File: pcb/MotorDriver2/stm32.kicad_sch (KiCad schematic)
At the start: 29 parts, among them IC1 STM32C092RCT6, J1 GT-USB-7010ASV, SW1 K2-6639SP-C4SC-04, SW2 K2-6639SP-C4SC-04, SW3 K2-6639SP-C4SC-04, U1 NCP361SNT1G, U2 CH340X, Y1 48 MHz, Y2 32.768 kHz

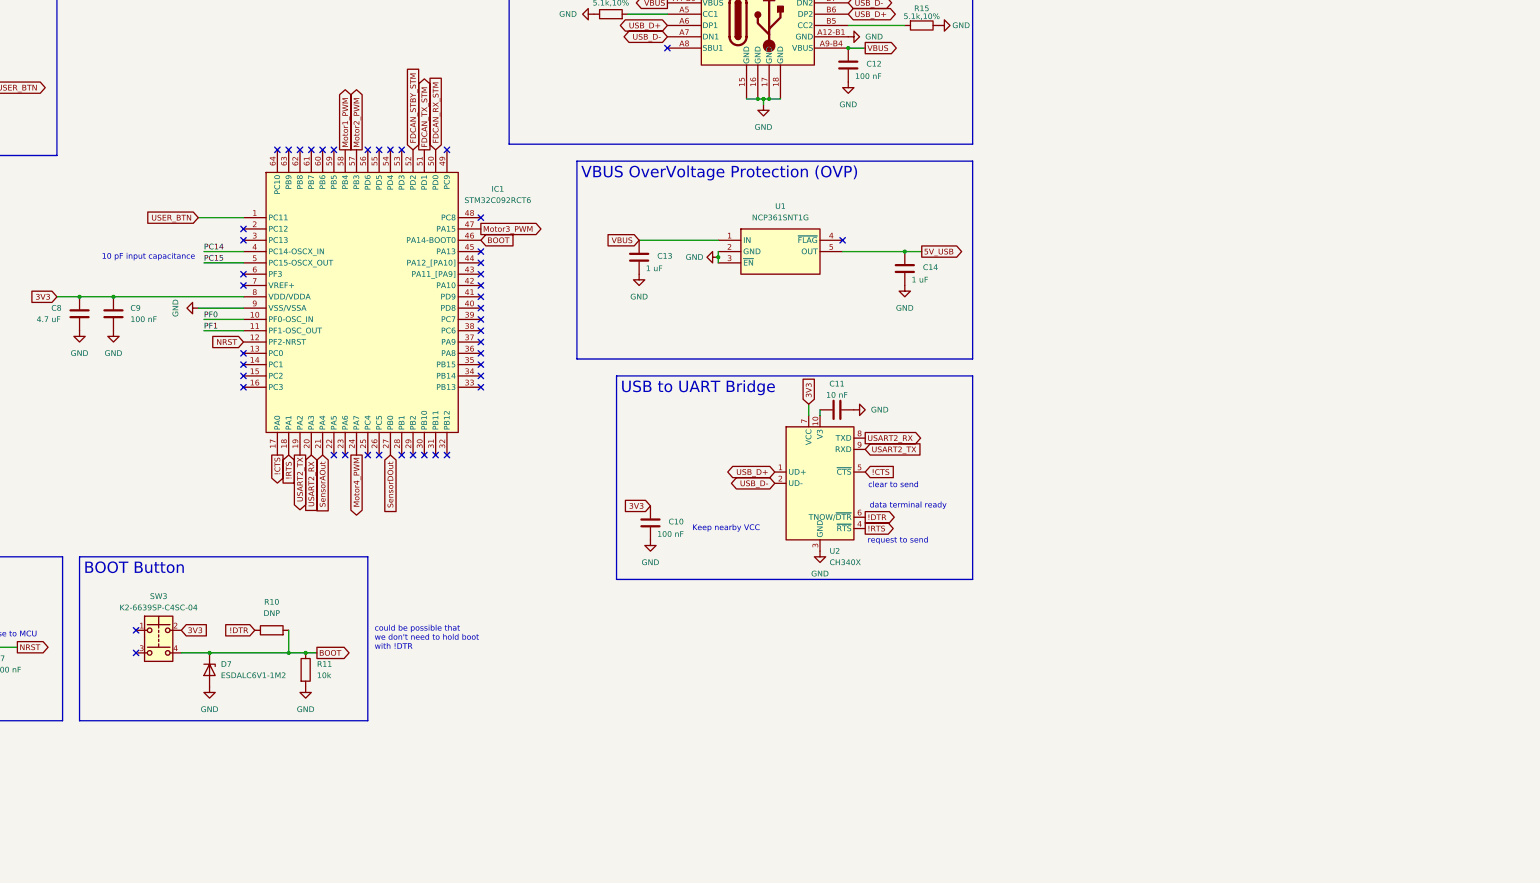
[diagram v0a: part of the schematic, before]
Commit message: Modifying usb uart schematic
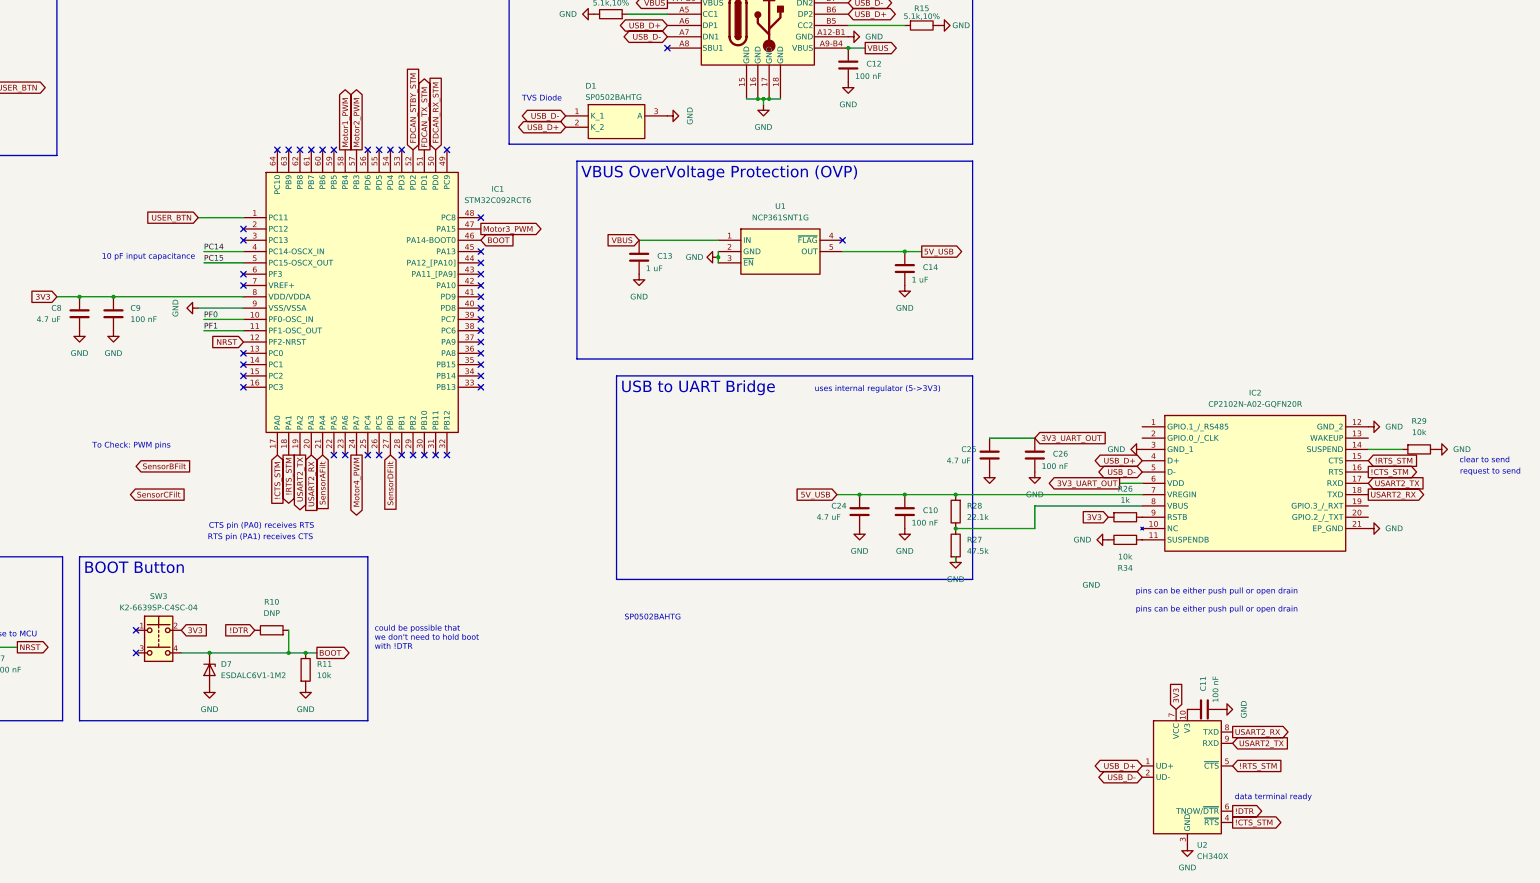
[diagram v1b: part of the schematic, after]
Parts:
- added C24, C25: 4.7 uF, Capacitor_SMD:C_0603_1608Metric, symbol Device:C
- added C26: 100 nF, Capacitor_SMD:C_0402_1005Metric, symbol Device:C
- added D1: SP0502BAHTG, CapstoneFootprints:SOT95P237X112-3N, symbol pcb:SP0502BAHTG
- added IC2: CP2102N-A02-GQFN20R, CapstoneFootprints:CP2102NA02GQFN20, symbol pcb:CP2102N-A02-GQFN20R
- added R26: 1k, Resistor_SMD:R_0402_1005Metric, symbol Device:R
- added R27: 47.5k, Resistor_SMD:R_0402_1005Metric, symbol Device:R
- added R28: 22.1k, Resistor_SMD:R_0402_1005Metric, symbol Device:R
- added R29, R34: 10k, Resistor_SMD:R_0402_1005Metric, symbol Device:R
- C11: value 10 nF -> 100 nF
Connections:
- net 3V3: now also R26.2; no longer C10.2
- net 5V_USB: now also C10.2, C24.2, IC2.7 (VREGIN), R28.2
- net GND: now also C11.1, C24.1, C25.1, C26.1, D1.3 (A), IC2.12 (GND_2), IC2.21 (EP_GND), IC2.3 (GND_1), R27.2, R29.1, R34.1; no longer C11.2
- net USART2_RX: now also IC2.18 (TXD)
- net USART2_TX: now also IC2.17 (RXD)
- net USB_D+: now also D1.2 (K_2), IC2.4 (D+)
- net USB_D-: now also D1.1 (K_1), IC2.5 (D-)
- net at U2.10 (V3): now also C11.2; no longer C11.1
- net !CTS renamed !CTS_STM
- net !CTS_STM: now also U2.4 (~{RTS}), IC2.16 (RTS); no longer U2.5 (~{CTS})
- net !RTS renamed !RTS_STM
- net !RTS_STM: now also U2.5 (~{CTS}), IC2.15 (CTS); no longer U2.4 (~{RTS})
- net SensorAOut renamed SensorAFilt
- net SensorDOut renamed SensorDFilt
- new net: IC2.14 (SUSPEND), R29.2
- new net: IC2.11 (SUSPENDB), R34.2
- new net: IC2.8 (VBUS), R27.1, R28.1
- new net: IC2.9 (RSTB), R26.1
- new net 3V3_UART_OUT: C25.2, C26.2, IC2.6 (VDD)
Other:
- note added: "CTS pin (PA0) receives RTS"
- note added: "RTS pin (PA1) receives CTS"
- note added: "SP0502BAHTG"
- note added: "TVS Diode"
- note added: "To Check: PWM pins"
- note added: "pins can be either push pull or open drain"
- note added: "uses internal regulator (5->3V3)"
- note removed: "Keep nearby VCC"
- moved on the sheet: C10

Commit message: Modified pwm pins
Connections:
- net Motor2a_PWM: now reaches IC1.25 (PC4)
- net Motor2b_PWM: now reaches IC1.26 (PC5)
- net Motor4a_PWM: now reaches IC1.42 (PA10)
- net Motor4b_PWM: now reaches IC1.61 (PB7)
- net Motor1_PWM renamed Motor3a_PWM
- net Motor2_PWM renamed Motor1b_PWM
- net Motor3_PWM renamed Motor1a_PWM
- net Motor4_PWM renamed Motor3b_PWM
- no-connect marks 52 -> 48
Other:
- note removed: "To Check: PWM pins"

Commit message: added ideal diode protection
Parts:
- removed C10, C11, C12, C26: 100 nF, Capacitor_SMD:C_0402_1005Metric, symbol Device:C
- removed C13, C14: 1 uF, Capacitor_SMD:C_0603_1608Metric, symbol Device:C
- removed C24, C25: 4.7 uF, Capacitor_SMD:C_0603_1608Metric, symbol Device:C
- removed D1: SP0502BAHTG, CapstoneFootprints:SOT95P237X112-3N, symbol pcb:SP0502BAHTG
- removed IC2: CP2102N-A02-GQFN20R, CapstoneFootprints:CP2102NA02GQFN20, symbol pcb:CP2102N-A02-GQFN20R
- removed J1: GT-USB-7010ASV, footprintLib:USB4110-GF-A_GCT, symbol pcb:USB4110-GF-A
- removed R12, R15: 5.1k,10%, Resistor_SMD:R_0402_1005Metric, symbol Device:R
- removed R26: 1k, Resistor_SMD:R_0402_1005Metric, symbol Device:R
- removed R27: 47.5k, Resistor_SMD:R_0402_1005Metric, symbol Device:R
- removed R28: 22.1k, Resistor_SMD:R_0402_1005Metric, symbol Device:R
- removed R29, R34: 10k, Resistor_SMD:R_0402_1005Metric, symbol Device:R
- removed U1: NCP361SNT1G, footprintLib:SOT95P275X110-5N, symbol pcb:NCP361SNT1G
- removed U2: CH340X, Package_SO:MSOP-10_3x3mm_P0.5mm, symbol Interface_USB:CH340X
- added TP1, TP2, TP3: TestPoint, TestPoint:TestPoint_Pad_1.0x1.0mm, symbol Connector:TestPoint
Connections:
- net SPI1_MISO: now also IC1.43 (PA11_[PA9]), TP2.1
- net SPI1_MOSI: now also IC1.44 (PA12_[PA10]), TP1.1
- net SensorBFilt: now also IC1.27 (PB0)
- net SensorCFilt: now also IC1.29 (PB2)
- net SensorDFilt: now also IC1.31 (PB11); no longer IC1.27 (PB0)
- net SPI1_SCK: now reaches IC1.40 (PD8)
- net SPI1_SCK: now also TP3.1
- no-connect marks 48 -> 40
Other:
- note removed: "SP0502BAHTG"
- note removed: "TVS Diode"
- note removed: "clear to send"
- note removed: "data terminal ready"
- note removed: "pins can be either push pull or open drain"
- note removed: "request to send"
- note removed: "uses internal regulator (5->3V3)"

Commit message: Laying out PCB
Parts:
- C3: LCSC (none) -> C3849295
- C5, C6: LCSC (none) -> C161334
- C7: LCSC (none) -> C1525
- C8: LCSC (none) -> C19666
- D5: LCSC (none) -> C2649894
- IC1: footprint footprintLib:QFP50P1200X1200X160-64N -> CapstoneFootprints:QFP50P1200X1200X160-64N
- SW1, SW2, SW3: footprint footprintLib:K2-6639SP-C4SC-04 -> CapstoneFootprints:K2-6639SP-C4SC-04
- Y1: footprint footprintLib:ECS-480-8-30-JGN-TR -> CapstoneFootprints:ECS-480-8-30-JGN-TR
- Y2: footprint footprintLib:MU00527-32.768K -> CapstoneFootprints:MU00527-32.768K
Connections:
- net Motor3a_PWM: now also IC1.39 (PC7); no longer IC1.58 (PB4)
- net Motor3b_PWM: now also IC1.38 (PC6); no longer IC1.24 (PA7)
- net Motor4a_PWM: now also IC1.60 (PB6); no longer IC1.42 (PA10)
- net SensorBFilt: now also IC1.28 (PB1); no longer IC1.27 (PB0)
- net SensorCFilt: now also IC1.30 (PB10); no longer IC1.29 (PB2)
- net SensorDFilt: now also IC1.32 (PB12); no longer IC1.31 (PB11)

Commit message: Finished pcb layout
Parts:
- removed R10: DNP, Resistor_SMD:R_0402_1005Metric, symbol Device:R
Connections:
- net SensorBFilt: now also IC1.22 (PA5); no longer IC1.28 (PB1)
- net SensorCFilt: now also IC1.23 (PA6); no longer IC1.30 (PB10)
- net SensorDFilt: now also IC1.24 (PA7); no longer IC1.32 (PB12)
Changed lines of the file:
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@@
 	)
 	(junction
-		(at 129.54 177.8)
-		(diameter 0)
-		(color 0 0 0 0)
-	)
-	(junction
 		(at 133.35 177.8)
 		(diameter 0)
@@
 	)
 	(no_connect
-		(at 144.78 133.35)
-	)
-	(no_connect
 		(at 132.08 64.77)
 	)
 	(no_connect
-		(at 139.7 133.35)
-	)
-	(no_connect
 		(at 119.38 115.57)
 	)
@@
 	)
 	(no_connect
+		(at 165.1 133.35)
+	)
+	(no_connect
 		(at 172.72 118.11)
 	)
@@
 	)
 	(no_connect
+		(at 154.94 133.35)
+	)
+	(no_connect
 		(at 172.72 110.49)
 	)
@@
 	)
 	(no_connect
-		(at 162.56 133.35)
+		(at 160.02 133.35)
 	)
 	(no_connect
@@
 	)
 	(no_connect
-		(at 172.72 115.57)
+		(at 162.56 133.35)
 	)
 	(no_connect
-		(at 154.94 64.77)
+		(at 172.72 115.57)
 	)
 	(no_connect
-		(at 142.24 133.35)
+		(at 154.94 64.77)
 	)
 	(no_connect
@@
 	(wire
 		(pts
-			(xy 111.76 177.8) (xy 129.54 177.8)
-		)
-		(stroke
-			(width 0)
-			(type default)
-		)
-	)
-	(wire
-		(pts
 			(xy 82.55 97.79) (xy 90.17 97.79)
 		)
@@
 	(wire
 		(pts
-			(xy 129.54 172.72) (xy 129.54 177.8)
-		)
-		(stroke
-			(width 0)
-			(type default)
-		)
-	)
-	(wire
-		(pts
 			(xy 33.02 50.8) (xy 39.37 50.8)
 		)
@@
 	(wire
 		(pts
-			(xy 129.54 177.8) (xy 133.35 177.8)
+			(xy 111.76 177.8) (xy 133.35 177.8)
 		)
 		(stroke
@@
 		)
 	)
-	(global_label "SensorBFilt"
-		(shape input)
-		(at 154.94 133.35 270)
-		(fields_autoplaced yes)
-		(effects
-			(font
-				(size 1.27 1.27)
-			)
-			(justify right)
-		)
-		(property "Intersheetrefs" "${INTERSHEET_REFS}"
-			(at 154.94 147.0999 90)
-			(effects
-				(font
-					(size 1.27 1.27)
-				)
-				(justify right)
-				(hide yes)
-			)
-		)
-	)
 	(global_label "Motor3a_PWM"
 		(shape input)
@@
 		)
 	)
-	(global_label "SensorDFilt"
-		(shape input)
-		(at 165.1 133.35 270)
-		(fields_autoplaced yes)
-		(effects
-			(font
-				(size 1.27 1.27)
-			)
-			(justify right)
-		)
-		(property "Intersheetrefs" "${INTERSHEET_REFS}"
-			(at 165.1 147.0999 90)
-			(effects
-				(font
-					(size 1.27 1.27)
-				)
-				(justify right)
-				(hide yes)
-			)
-		)
-	)
 	(global_label "3V3"
 		(shape input)
@@
 		)
 	)
-	(global_label "SensorCFilt"
+	(global_label "SensorBFilt"
 		(shape input)
-		(at 160.02 133.35 270)
+		(at 139.7 133.35 270)
 		(fields_autoplaced yes)
 		(effects
@@
 		)
 		(property "Intersheetrefs" "${INTERSHEET_REFS}"
-			(at 160.02 147.0999 90)
+			(at 139.7 147.0999 90)
 			(effects
 				(font
@@
 		)
 	)
-	(global_label "!DTR"
-		(shape input)
-		(at 121.92 172.72 180)
-		(fields_autoplaced yes)
-		(effects
-			(font
-				(size 1.27 1.27)
-			)
-			(justify right)
-		)
-		(property "Intersheetrefs" "${INTERSHEET_REFS}"
-			(at 114.8224 172.72 0)
-			(effects
-				(font
-					(size 1.27 1.27)
-				)
-				(justify right)
-				(hide yes)
-			)
-		)
-	)
 	(global_label "!RTS_STM"
 		(shape output)
@@
 		)
 	)
+	(global_label "SensorCFilt"
+		(shape input)
+		(at 142.24 133.35 270)
+		(fields_autoplaced yes)
+		(effects
+			(font
+				(size 1.27 1.27)
+			)
+			(justify right)
+		)
+		(property "Intersheetrefs" "${INTERSHEET_REFS}"
+			(at 142.24 147.0999 90)
+			(effects
+				(font
+					(size 1.27 1.27)
+				)
+				(justify right)
+				(hide yes)
+			)
+		)
+	)
+	(global_label "SensorDFilt"
+		(shape input)
+		(at 144.78 133.35 270)
+		(fields_autoplaced yes)
+		(effects
+			(font
+				(size 1.27 1.27)
+			)
+			(justify right)
+		)
+		(property "Intersheetrefs" "${INTERSHEET_REFS}"
+			(at 144.78 147.0999 90)
+			(effects
+				(font
+					(size 1.27 1.27)
+				)
+				(justify right)
+				(hide yes)
+			)
+		)
+	)
 	(global_label "Motor2a_PWM"
 		(shape input)
@@
 					(unit 1)
 				)
-			)
-		)
-	)
-	(symbol
-		(lib_id "Device:R")
-		(at 125.73 172.72 90)
-		(unit 1)
-		(exclude_from_sim no)
-		(in_bom yes)
-		(on_board yes)
-		(dnp no)
-		(fields_autoplaced yes)
-		(property "Reference" "R10"
-			(at 125.73 166.37 90)
-			(effects
-				(font
-					(size 1.27 1.27)
-				)
-			)
-		)
-		(property "Value" "DNP"
-			(at 125.73 168.91 90)
-			(effects
-				(font
-					(size 1.27 1.27)
-				)
-			)
-		)
-		(property "Footprint" "Resistor_SMD:R_0402_1005Metric"
-			(at 125.73 174.498 90)
-			(effects
-				(font
-					(size 1.27 1.27)
-				)
-				(hide yes)
-			)
-		)
-		(property "Datasheet" "~"
-			(at 125.73 172.72 0)
-			(effects
-				(font
-					(size 1.27 1.27)
-				)
-				(hide yes)
-			)
-		)
-		(property "Description" "Resistor"
-			(at 125.73 172.72 0)
-			(effects
-				(font
-					(size 1.27 1.27)
-				)
-				(hide yes)
-			)
-		)
-		(pin "1"
-		)
-		(pin "2"
-		)
-		(instances
-			(project "MotorDriver1"
-				(path "/6e0510ec-6dbc-4bc1-a315-3680b1127a92/06299a0e-39a9-4081-8894-5693d9896b0f"
-					(reference "R10")
-					(unit 1)
-				)
-			)
-			(project "MotorDriver1"
-				(path "/79cc9cfe-04d6-4d00-aa84-feae66cf8c45/d5cdf697-4d49-4f45-b387-9e9064a8239b"
-					(reference "R10")
-					(unit 1)
-				)

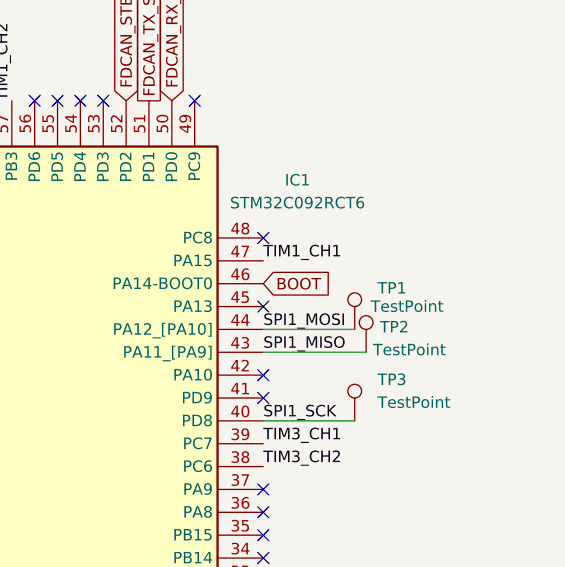
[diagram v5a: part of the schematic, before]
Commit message: Added STLink Connector
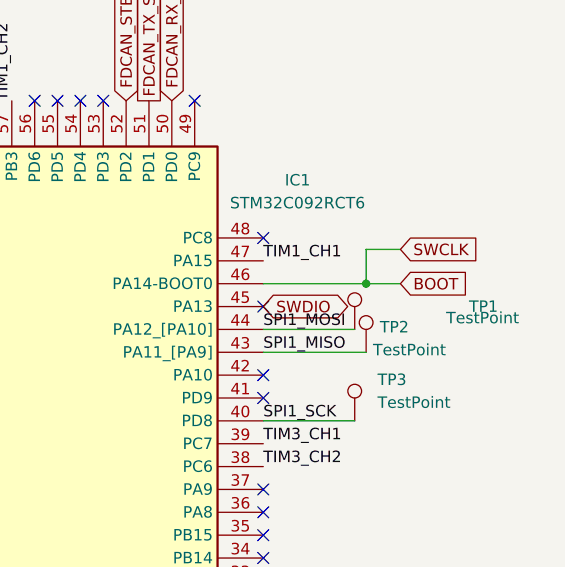
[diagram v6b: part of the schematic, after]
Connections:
- net SWDIO: now reaches IC1.45 (PA13)
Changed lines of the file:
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@@
 	)
 	(junction
+		(at 184.15 85.09)
+		(diameter 0)
+		(color 0 0 0 0)
+	)
+	(junction
 		(at 35.56 83.82)
 		(diameter 0)
@@
 	(wire
 		(pts
+			(xy 187.96 81.28) (xy 184.15 81.28)
+		)
+		(stroke
+			(width 0)
+			(type default)
+		)
+	)
+	(wire
+		(pts
+			(xy 172.72 85.09) (xy 184.15 85.09)
+		)
+		(stroke
+			(width 0)
+			(type default)
+		)
+	)
+	(wire
+		(pts
 			(xy 82.55 97.79) (xy 90.17 97.79)
 		)
@@
 	(wire
 		(pts
+			(xy 184.15 81.28) (xy 184.15 85.09)
+		)
+		(stroke
+			(width 0)
+			(type default)
+		)
+	)
+	(wire
+		(pts
 			(xy 33.02 50.8) (xy 39.37 50.8)
 		)
@@
 	(wire
 		(pts
+			(xy 184.15 85.09) (xy 187.96 85.09)
+		)
+		(stroke
+			(width 0)
+			(type default)
+		)
+	)
+	(wire
+		(pts
 			(xy 109.22 80.01) (xy 119.38 80.01)
 		)
@@
 		)
 	)
+	(global_label "SWCLK"
+		(shape input)
+		(at 187.96 81.28 0)
+		(fields_autoplaced yes)
+		(effects
+			(font
+				(size 1.27 1.27)
+			)
+			(justify left)
+		)
+		(property "Intersheetrefs" "${INTERSHEET_REFS}"
+			(at 197.1742 81.28 0)
+			(effects
+				(font
+					(size 1.27 1.27)
+				)
+				(justify left)
+				(hide yes)
+			)
+		)
+	)
 	(global_label "3V3"
 		(shape input)
@@
 		)
 	)
+	(global_label "SWDIO"
+		(shape bidirectional)
+		(at 172.72 87.63 0)
+		(fields_autoplaced yes)
+		(effects
+			(font
+				(size 1.27 1.27)
+			)
+			(justify left)
+		)
+		(property "Intersheetrefs" "${INTERSHEET_REFS}"
+			(at 182.6827 87.63 0)
+			(effects
+				(font
+					(size 1.27 1.27)
+				)
+				(justify left)
+				(hide yes)
+			)
+		)
+	)
 	(global_label "Motor1b_PWM"
 		(shape input)
@@
 	(global_label "BOOT"
 		(shape input)
-		(at 172.72 85.09 0)
+		(at 187.96 85.09 0)
 		(fields_autoplaced yes)
 		(effects
@@
 		)
 		(property "Intersheetrefs" "${INTERSHEET_REFS}"
-			(at 180.6038 85.09 0)
+			(at 195.8438 85.09 0)
 			(effects
 				(font
@@
 				)
 			)
+			(project "stm32"
+				(path "/85f32bc1-9169-480e-a658-3b951d4944e0"
+					(reference "D?")
+					(unit 1)
+				)
+			)
 		)
 	)
@@
 				)
 			)
+			(project "stm32"
+				(path "/85f32bc1-9169-480e-a658-3b951d4944e0"
+					(reference "#PWR?")
+					(unit 1)
+				)
+			)
 		)
 	)
@@
 				)
 			)
+			(project "stm32"
+				(path "/85f32bc1-9169-480e-a658-3b951d4944e0"
+					(reference "SW?")
+					(unit 1)
+				)
+			)
 		)
 	)
@@
 				)
 			)
+			(project "stm32"
+				(path "/85f32bc1-9169-480e-a658-3b951d4944e0"
+					(reference "R?")
+					(unit 1)
+				)
+			)
 		)
 	)
@@
 				)
 			)
+			(project "stm32"
+				(path "/85f32bc1-9169-480e-a658-3b951d4944e0"
+					(reference "SW?")
+					(unit 1)
+				)
+			)
 		)
 	)
@@
 				)
 			)
+			(project "stm32"
+				(path "/85f32bc1-9169-480e-a658-3b951d4944e0"
+					(reference "#PWR?")
+					(unit 1)
+				)
+			)
 		)
 	)
@@
 				)
 			)
+			(project "stm32"
+				(path "/85f32bc1-9169-480e-a658-3b951d4944e0"
+					(reference "TP?")
+					(unit 1)
+				)
+			)
 		)
 	)
@@
 				)
 			)
+			(project "stm32"
+				(path "/85f32bc1-9169-480e-a658-3b951d4944e0"
+					(reference "R?")
+					(unit 1)
+				)
+			)
 		)
 	)
@@
 				)
 			)
+			(project "stm32"
+				(path "/85f32bc1-9169-480e-a658-3b951d4944e0"
+					(reference "#PWR?")
+					(unit 1)
+				)
+			)
 		)
 	)
@@
 				)
 			)
+			(project "stm32"
+				(path "/85f32bc1-9169-480e-a658-3b951d4944e0"
+					(reference "TP?")
+					(unit 1)
+				)
+			)
 		)
 	)
@@
 		(dnp no)
 		(property "Reference" "TP1"
-			(at 185.42 85.5979 0)
+			(at 195.58 87.63 0)
 			(effects
 				(font
@@
 		)
 		(property "Value" "TestPoint"
-			(at 184.658 87.63 0)
+			(at 193.04 88.9 0)
 			(effects
 				(font
@@
 				)
 			)
+			(project "stm32"
+				(path "/85f32bc1-9169-480e-a658-3b951d4944e0"
+					(reference "TP?")
+					(unit 1)
+				)
+			)
 		)
 	)
@@
 				)
 			)
+			(project "stm32"
+				(path "/85f32bc1-9169-480e-a658-3b951d4944e0"
+					(reference "D?")
+					(unit 1)
+				)
+			)
 		)
 	)
@@
 		)
 	)
+	(sheet_instances
+		(path "/"
+			(page "1")
+		)
+	)
+	(embedded_fonts no)
 )
